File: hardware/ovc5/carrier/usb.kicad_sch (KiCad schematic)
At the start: 107 parts, among them J1 USB_C_Receptacle, U10 S25FL064, U2 CYUSB43x7, U5 USB3_A_Dual_Stacked, U8 TPS2561, Y1 25MHz

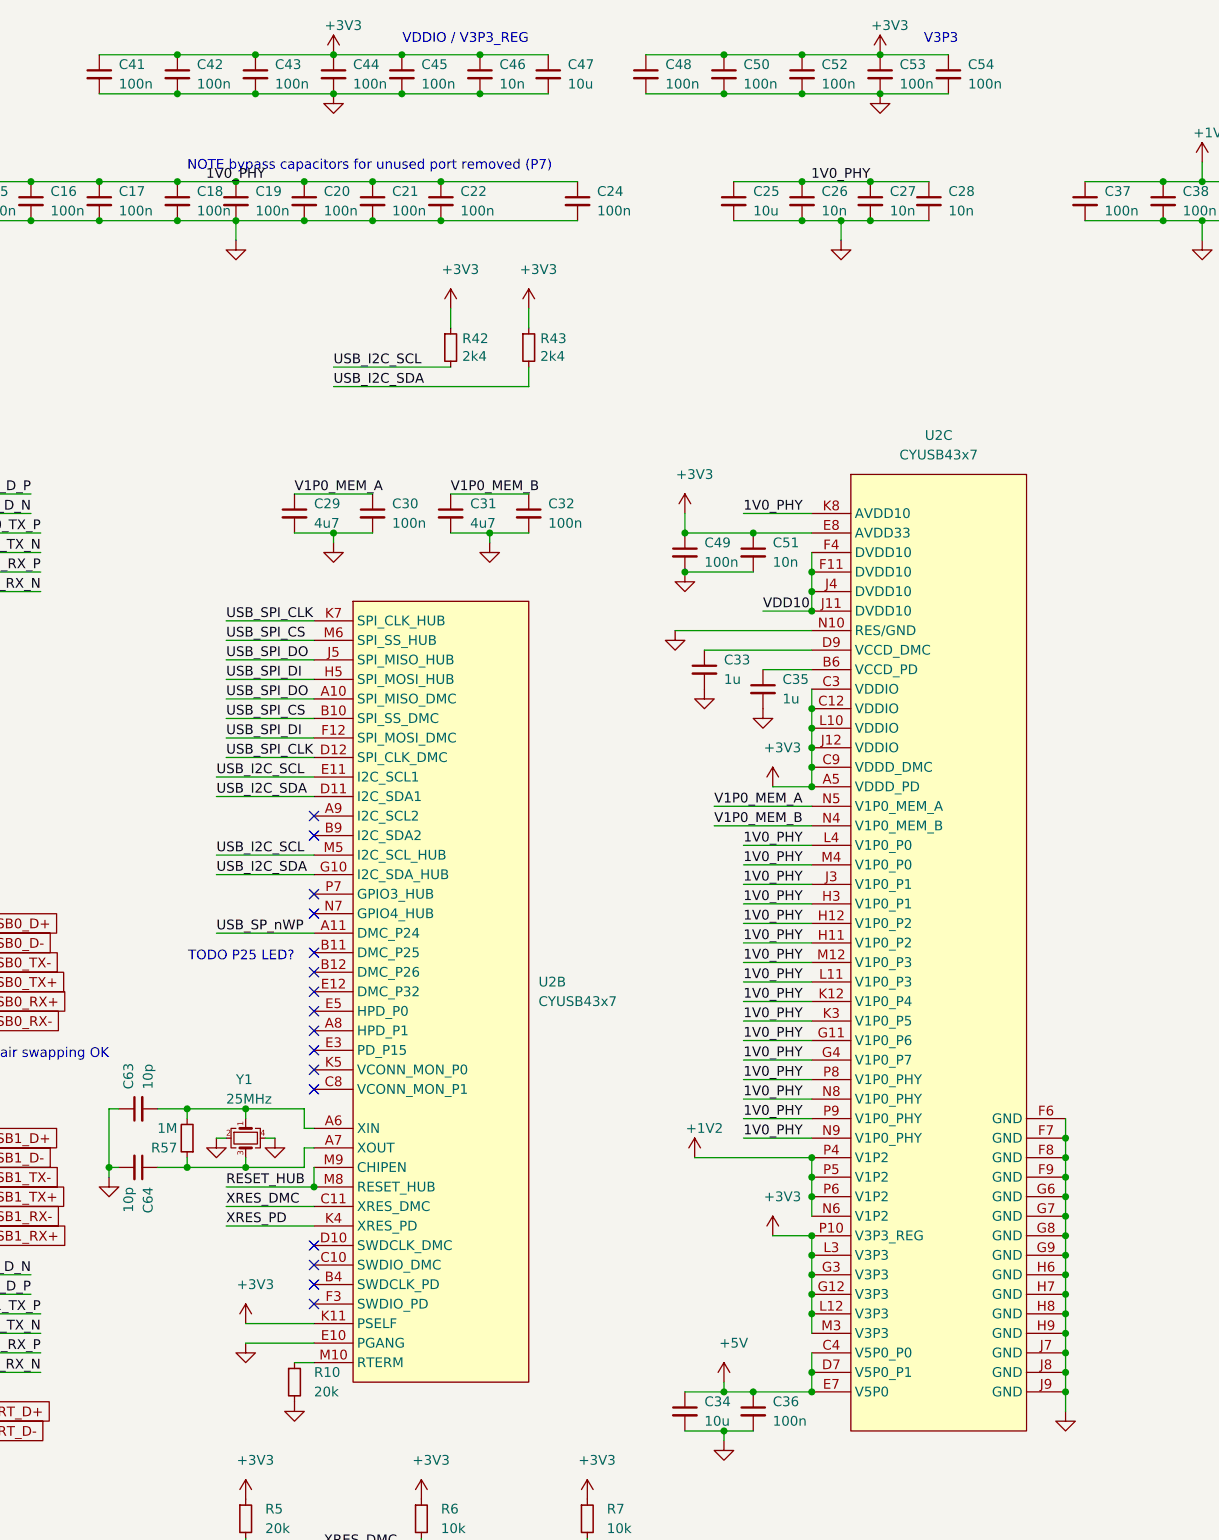
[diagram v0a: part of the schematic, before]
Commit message: Redo layout of BGA WIP
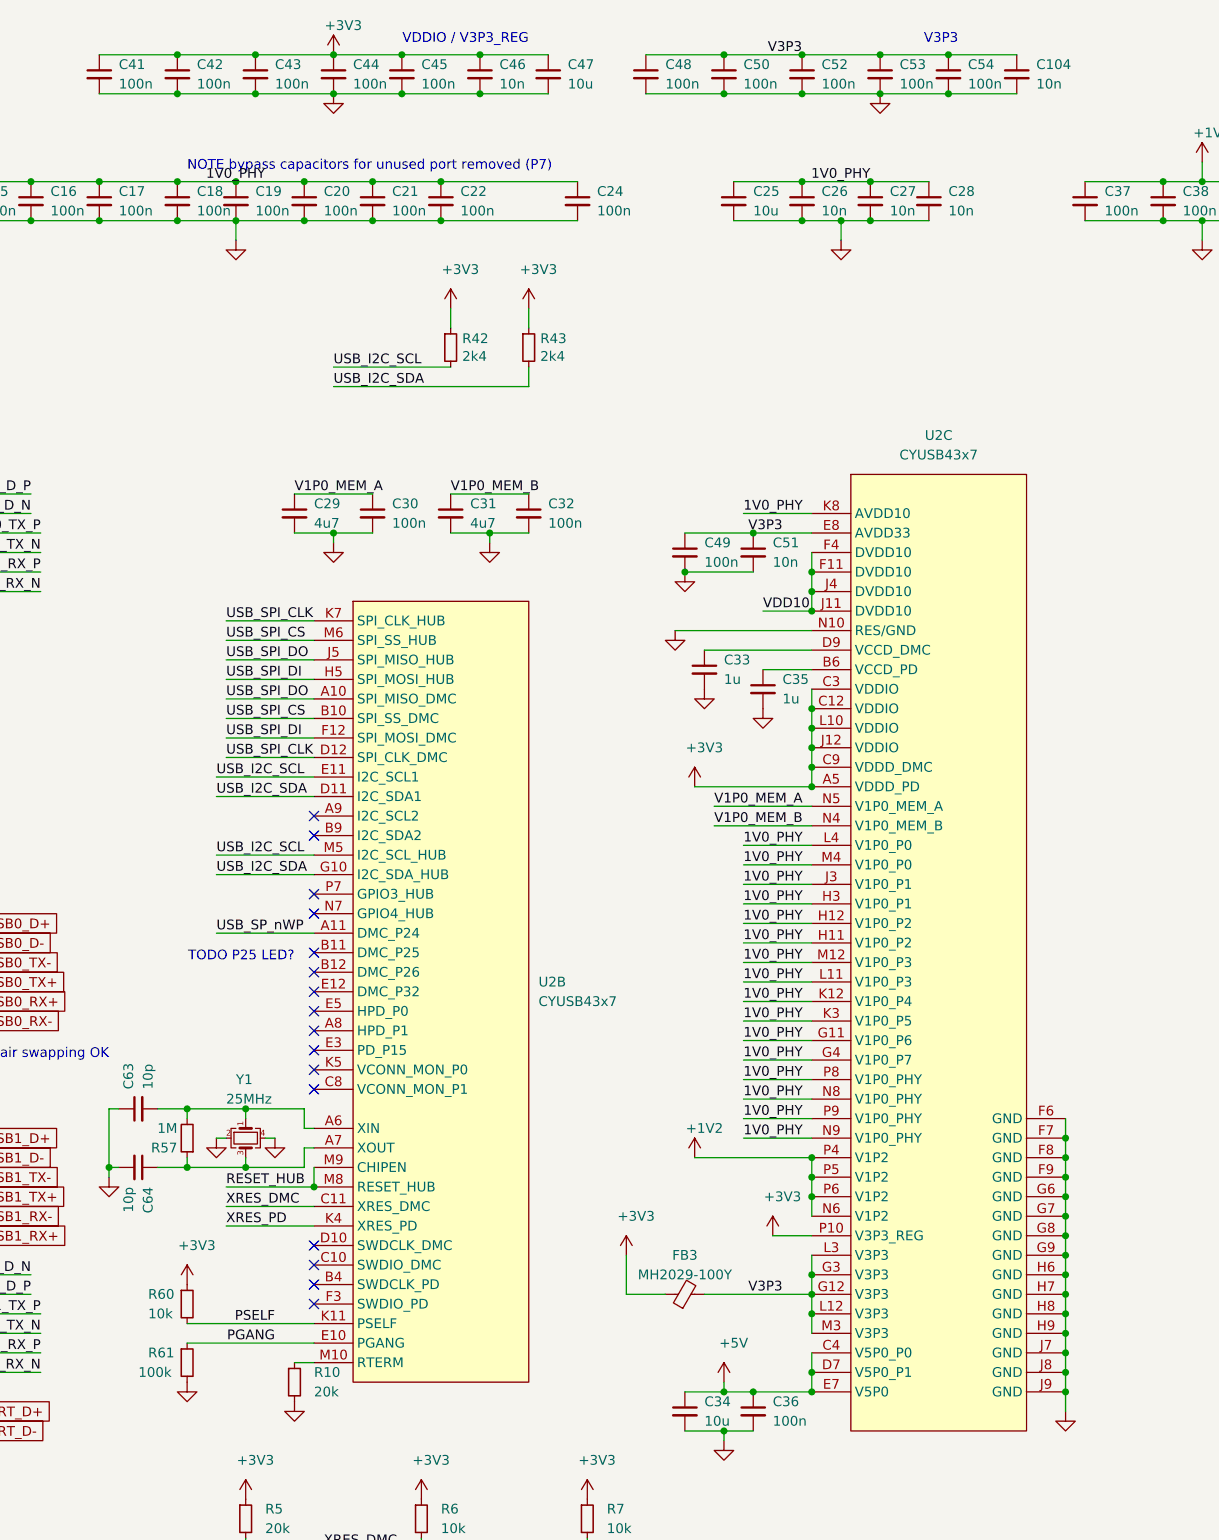
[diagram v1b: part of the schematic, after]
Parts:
- added C104: 10n, Capacitor_SMD:C_0402_1005Metric, symbol Device:C_Small
- added FB3: MH2029-100Y, Inductor_SMD:L_0805_2012Metric, symbol Device:FerriteBead_Small
- added R60: 10k, Resistor_SMD:R_0402_1005Metric, symbol Device:R_Small
- added R61: 100k, Resistor_SMD:R_0402_1005Metric, symbol Device:R_Small
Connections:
- net +3V3: now also FB3.1, R60.1; no longer C48.1, C49.1, C50.1, C51.1, C52.1, C53.1, C54.1, U2.E8 (AVDD33), U2.G12 (V3P3), U2.G3 (V3P3), U2.K11 (PSELF), U2.L12 (V3P3), U2.L3 (V3P3), U2.M3 (V3P3)
- net GND: now also C104.2, R61.2; no longer U2.E10 (PGANG)
- new net PGANG: R61.1, U2.E10 (PGANG)
- new net PSELF: R60.2, U2.K11 (PSELF)
- new net V3P3: C104.1, C48.1, C49.1, C50.1, C51.1, C52.1, C53.1, C54.1, FB3.2, U2.E8 (AVDD33), U2.G12 (V3P3), U2.G3 (V3P3), U2.L12 (V3P3), U2.L3 (V3P3), U2.M3 (V3P3)
